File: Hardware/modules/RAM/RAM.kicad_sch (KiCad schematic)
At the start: 7 parts, among them J1 Bus_PCI_6502, U1 AS6C4008-55PCN, U2 CY62256-70PC

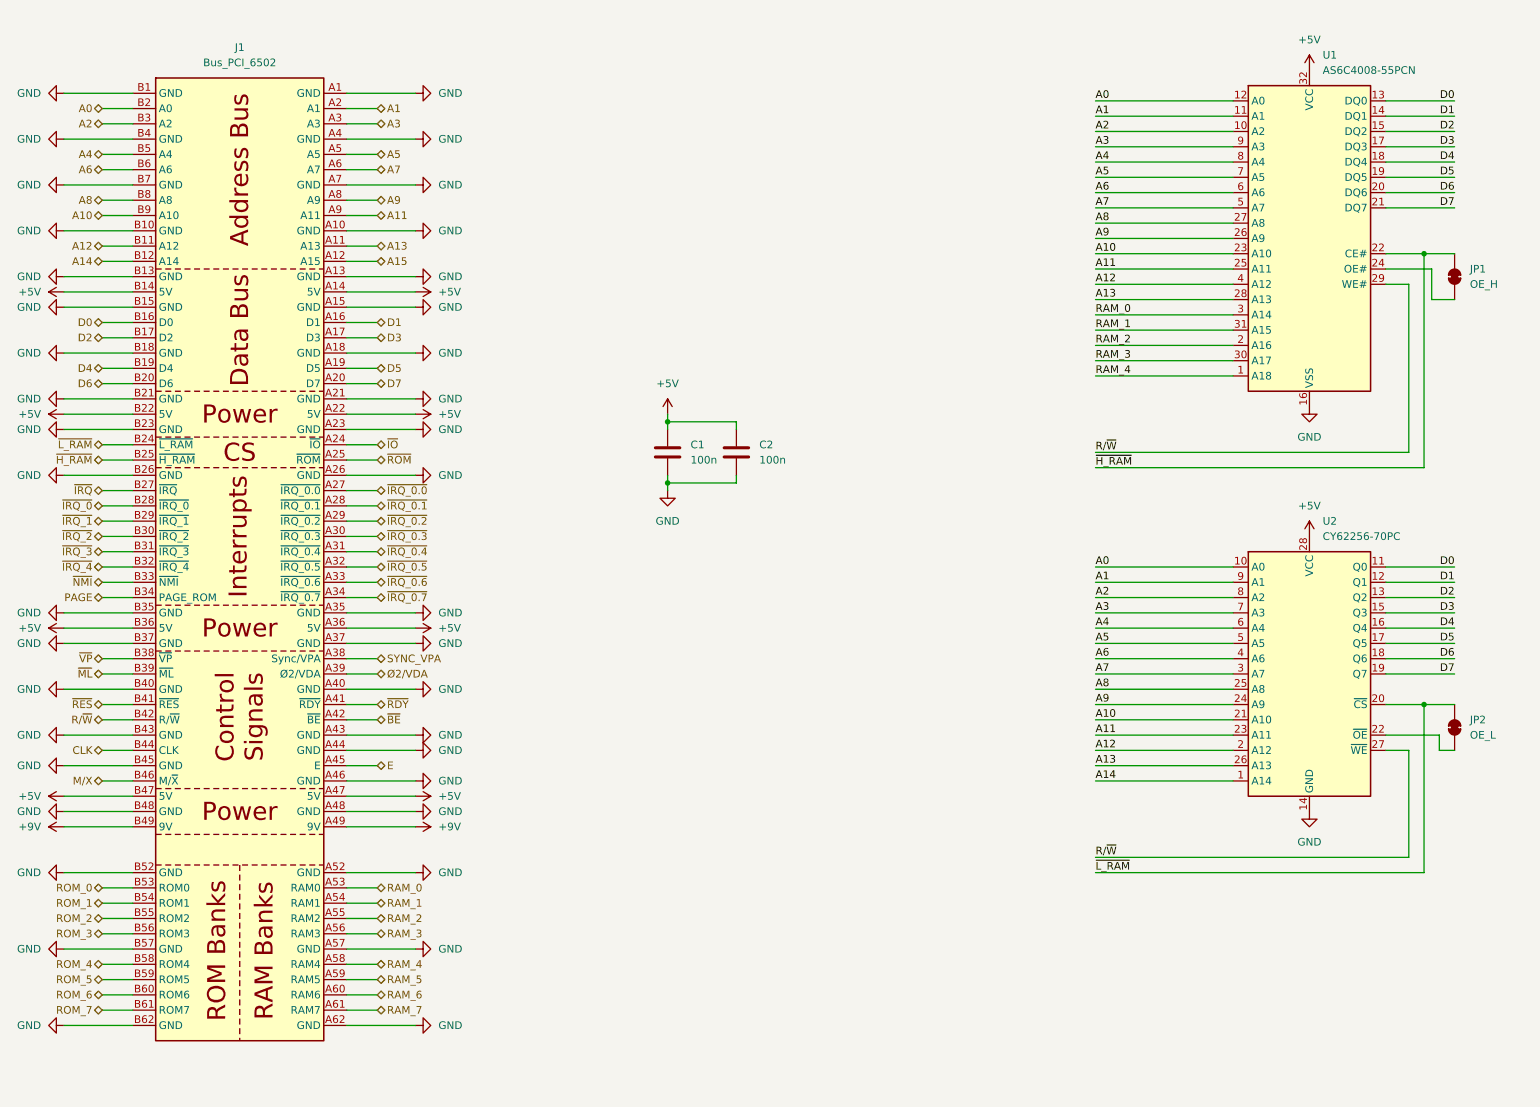
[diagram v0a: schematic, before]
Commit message: Hardware Update Add MyCPU VGA Module Beautify all Schematics minor Error corrections Readme Update
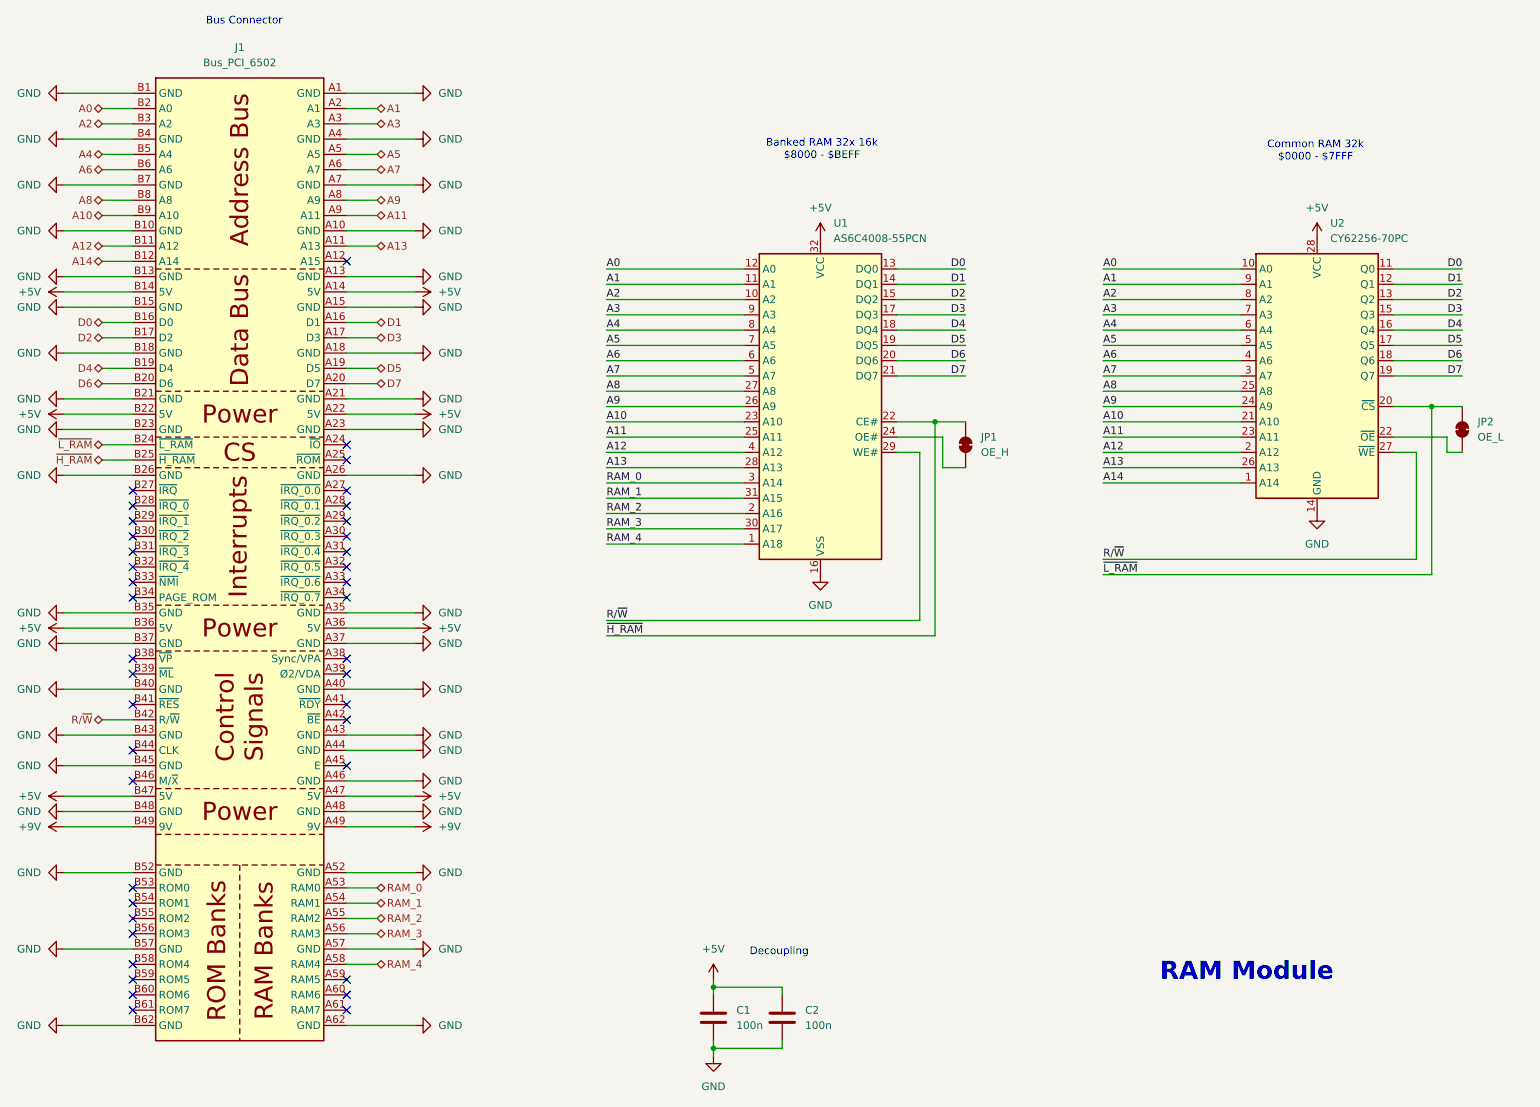
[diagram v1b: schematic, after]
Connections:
- net A15: no longer names the net of J1.A12 (A15)
- net CLK: no longer names the net of J1.B44 (CLK)
- net E: no longer names the net of J1.A45 (E)
- net M/X: no longer names the net of J1.B46 (M/~{X})
- net PAGE: no longer names the net of J1.B34 (PAGE_ROM)
- net RAM_5: no longer names the net of J1.A59 (RAM5)
- net RAM_6: no longer names the net of J1.A60 (RAM6)
- net RAM_7: no longer names the net of J1.A61 (RAM7)
- net ROM_0: no longer names the net of J1.B53 (ROM0)
- net ROM_1: no longer names the net of J1.B54 (ROM1)
- net ROM_2: no longer names the net of J1.B55 (ROM2)
- net ROM_3: no longer names the net of J1.B56 (ROM3)
- net ROM_4: no longer names the net of J1.B58 (ROM4)
- net ROM_5: no longer names the net of J1.B59 (ROM5)
- net ROM_6: no longer names the net of J1.B60 (ROM6)
- net ROM_7: no longer names the net of J1.B61 (ROM7)
- net SYNC_VPA: no longer names the net of J1.A38 (Sync/VPA)
- net ~{BE}: no longer names the net of J1.A42 (~{BE})
- net ~{IO}: no longer names the net of J1.A24 (~{IO})
- net ~{IRQ_0.0}: no longer names the net of J1.A27 (~{IRQ_0.0})
- net ~{IRQ_0.1}: no longer names the net of J1.A28 (~{IRQ_0.1})
- net ~{IRQ_0.2}: no longer names the net of J1.A29 (~{IRQ_0.2})
- net ~{IRQ_0.3}: no longer names the net of J1.A30 (~{IRQ_0.3})
- net ~{IRQ_0.4}: no longer names the net of J1.A31 (~{IRQ_0.4})
- net ~{IRQ_0.5}: no longer names the net of J1.A32 (~{IRQ_0.5})
- net ~{IRQ_0.6}: no longer names the net of J1.A33 (~{IRQ_0.6})
- net ~{IRQ_0.7}: no longer names the net of J1.A34 (~{IRQ_0.7})
- net ~{IRQ_0}: no longer names the net of J1.B28 (~{IRQ_0})
- net ~{IRQ_1}: no longer names the net of J1.B29 (~{IRQ_1})
- net ~{IRQ_2}: no longer names the net of J1.B30 (~{IRQ_2})
- net ~{IRQ_3}: no longer names the net of J1.B31 (~{IRQ_3})
- net ~{IRQ_4}: no longer names the net of J1.B32 (~{IRQ_4})
- net ~{IRQ}: no longer names the net of J1.B27 (~{IRQ})
- net ~{ML}: no longer names the net of J1.B39 (~{ML})
- net ~{NMI}: no longer names the net of J1.B33 (~{NMI})
- net ~{RDY}: no longer names the net of J1.A41 (~{RDY})
- net ~{RES}: no longer names the net of J1.B41 (~{RES})
- net ~{ROM}: no longer names the net of J1.A25 (~{ROM})
- net ~{VP}: no longer names the net of J1.B38 (~{VP})
- net Ø2/VDA: no longer names the net of J1.A39 (Ø2/VDA)
- no-connect marks 0 -> 40
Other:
- note added: "Banked RAM 32x 16k $8000 - $BEFF"
- note added: "Bus Connector"
- note added: "Common RAM 32k $0000 - $7FFF"
- note added: "Decoupling"
- note added: "RAM Module"
- company: (none) -> Synthron
- title: (none) -> S65xx Computer System
- moved on the sheet: C1, C2, JP1, JP2, U1, U2

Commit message: Fix mirroring on High-Ram on Bank Select
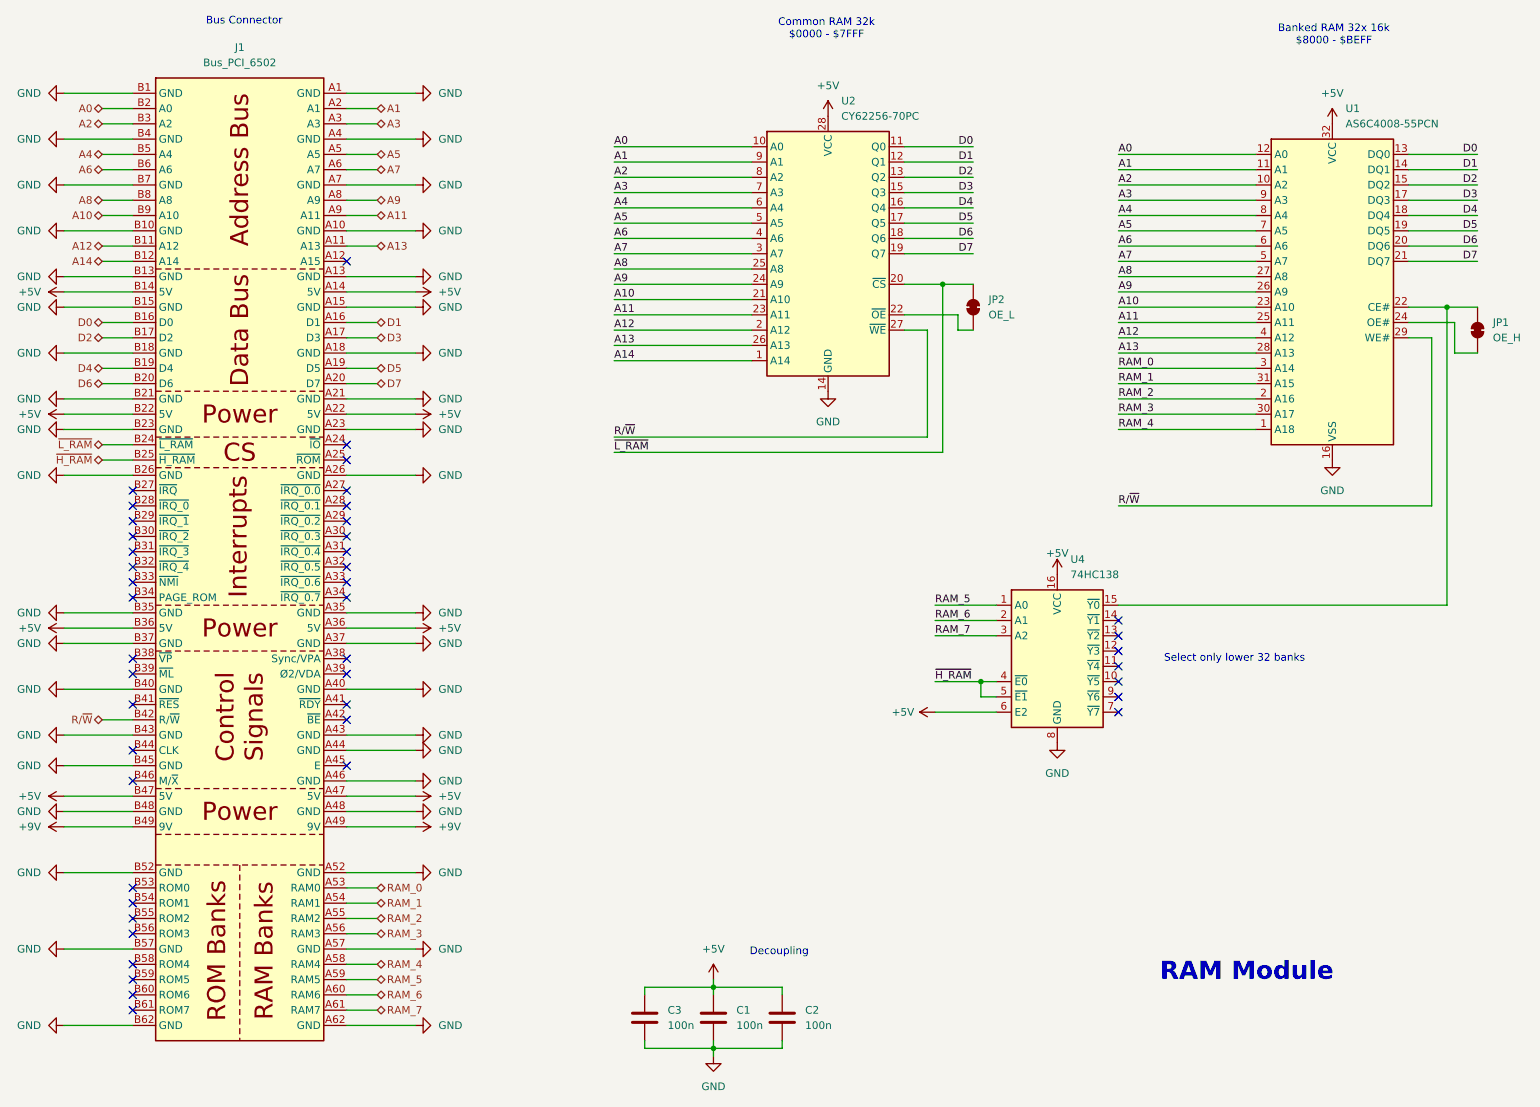
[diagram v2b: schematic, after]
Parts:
- added C3: 100n, Capacitor_SMD:C_0805_2012Metric, symbol Device:C
- added U4: 74HC138, Package_DIP:DIP-16_W7.62mm, symbol 74xx:74HC138
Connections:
- net +5V: now also C3.1, U4.16 (VCC), U4.6 (E2)
- net GND: now also C3.2, U4.8 (GND)
- net ~{H_RAM}: now also U4.4 (~{E0}), U4.5 (~{E1}); no longer JP1.2 (B), U1.22 (CE#)
- net RAM_5: now reaches J1.A59 (RAM5)
- net RAM_5: now also U4.1 (A0)
- net RAM_6: now reaches J1.A60 (RAM6)
- net RAM_6: now also U4.2 (A1)
- net RAM_7: now reaches J1.A61 (RAM7)
- net RAM_7: now also U4.3 (A2)
- new net: JP1.2 (B), U1.22 (CE#), U4.15 (~{Y0})
- no-connect marks 40 -> 44
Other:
- note added: "Select only lower 32 banks"
- moved on the sheet: JP1, JP2, U1, U2

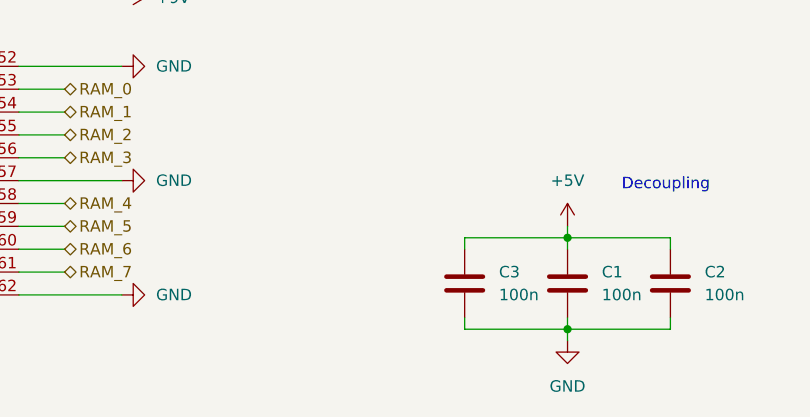
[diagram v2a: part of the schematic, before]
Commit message: Hardware Review Pt. 1 fix Address Decoding for Strobe Generators add bulk capacitance to every board fix wiring of Prototyping Board
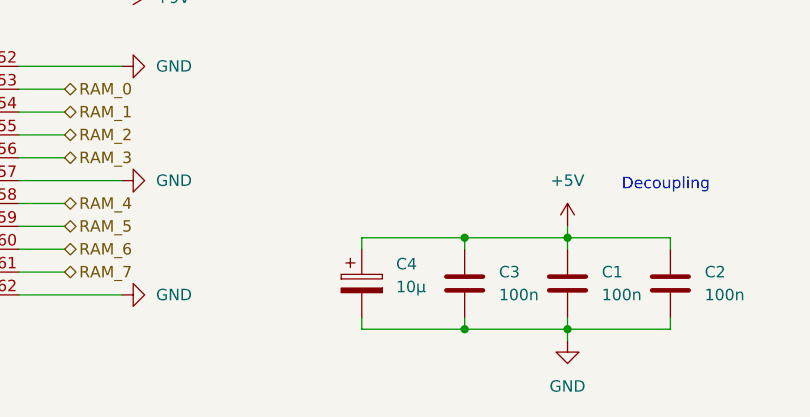
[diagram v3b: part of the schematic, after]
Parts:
- added C4: 10µ, Capacitor_THT:CP_Radial_D5.0mm_P2.50mm, symbol Device:C_Polarized
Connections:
- net +5V: now also C4.1
- net GND: now also C4.2
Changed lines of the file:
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@@
+	)
+	(junction
+		(at 129.54 187.96)
+		(diameter 0)
+		(color 0 0 0 0)
 	)
 	(junction
@@
 	)
 	(junction
+		(at 129.54 177.8)
+		(diameter 0)
+		(color 0 0 0 0)
+	)
+	(junction
 		(at 185.42 127)
 		(diameter 0)
@@
 	(wire
 		(pts
+			(xy 118.11 179.07) (xy 118.11 177.8)
+		)
+		(stroke
+			(width 0)
+			(type default)
+		)
+	)
+	(wire
+		(pts
 			(xy 140.97 187.96) (xy 140.97 189.23)
 		)
@@
 	(wire
 		(pts
+			(xy 118.11 187.96) (xy 129.54 187.96)
+		)
+		(stroke
+			(width 0)
+			(type default)
+		)
+	)
+	(wire
+		(pts
 			(xy 177.8 114.3) (xy 187.96 114.3)
 		)
@@
 	(wire
 		(pts
+			(xy 118.11 186.69) (xy 118.11 187.96)
+		)
+		(stroke
+			(width 0)
+			(type default)
+		)
+	)
+	(wire
+		(pts
 			(xy 176.53 68.58) (xy 172.72 68.58)
 		)
@@
 		(pts
 			(xy 80.01 176.53) (xy 85.09 176.53)
+		)
+		(stroke
+			(width 0)
+			(type default)
+		)
+	)
+	(wire
+		(pts
+			(xy 118.11 177.8) (xy 129.54 177.8)
 		)
 		(stroke
@@
 		)
 	)
+	(symbol
+		(lib_id "Device:C_Polarized")
+		(at 118.11 182.88 0)
+		(unit 1)
+		(exclude_from_sim no)
+		(in_bom yes)
+		(on_board yes)
+		(dnp no)
+		(fields_autoplaced yes)
+		(property "Reference" "C4"
+			(at 121.92 180.7209 0)
+			(effects
+				(font
+					(size 1.27 1.27)
+				)
+				(justify left)
+			)
+		)
+		(property "Value" "10µ"
+			(at 121.92 183.2609 0)
+			(effects
+				(font
+					(size 1.27 1.27)
+				)
+				(justify left)
+			)
+		)
+		(property "Footprint" "Capacitor_THT:CP_Radial_D5.0mm_P2.50mm"
+			(at 119.0752 186.69 0)
+			(effects
+				(font
+					(size 1.27 1.27)
+				)
+				(hide yes)
+			)
+		)
+		(property "Datasheet" "~"
+			(at 118.11 182.88 0)
+			(effects
+				(font
+					(size 1.27 1.27)
+				)
+				(hide yes)
+			)
+		)
+		(property "Description" "Polarized capacitor"
+			(at 118.11 182.88 0)
+			(effects
+				(font
+					(size 1.27 1.27)
+				)
+				(hide yes)
+			)
+		)
+		(pin "2"
+		)
+		(pin "1"
+		)
+		(instances
+			(project ""
+				(path "/bd1fe73d-f8a9-4348-8266-6b95f5996cdd"
+					(reference "C4")
+					(unit 1)
+				)
+			)
+		)
+	)
